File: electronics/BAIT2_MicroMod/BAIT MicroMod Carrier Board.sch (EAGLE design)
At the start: 152 parts, among them J1 SJ-43516-SMT, J10 QWIIC_RIGHT_ANGLE, J15 SM06B-SRSS-TB(LF)(SN), J2 ST-TF-003A, J4 JST_6_PIN_VERTICAL, J5 QWIIC_RIGHT_ANGLE, J6 JST 2PH, J7 MICROMOD-2222-C, SW1 SKQGADE010, SW2 SKQGADE010, U1 SGTL5000-32, U10 TSL25911, U2 AP7313, U3 3.3V, U4 3.3V, U5 BQ27441-G1, U6 BQ24074, U7 LoRa-E5-HF, U8 S-1172B33-E6T1U, U9 BOSCH_TOOLS_BME680BOSCH_TOOLS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

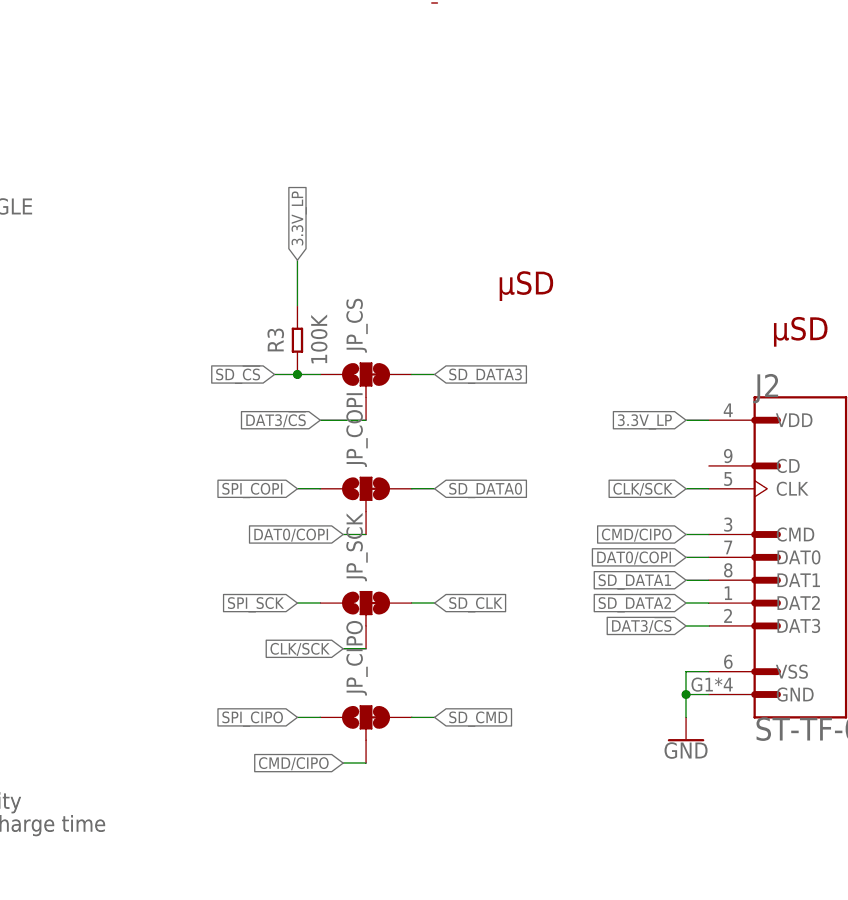
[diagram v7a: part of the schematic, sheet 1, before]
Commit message: Removes secondary options for connecting to SD card
Resolves #22
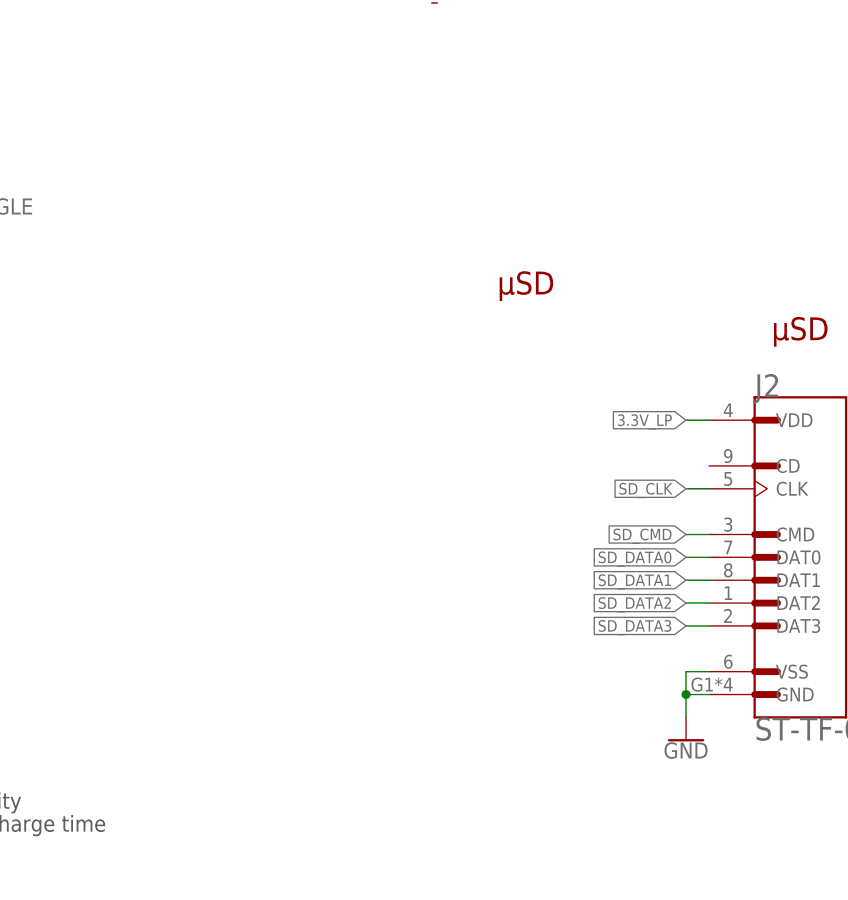
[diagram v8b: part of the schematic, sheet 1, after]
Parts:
- removed JP_CIPO, JP_COPI, JP_CS, JP_SCK: JUMPER-SMT_3_1-NC_TRACE_SILK, SparkFun-Jumpers:JUMPER-SMT_3_1-NC_TRACE_SILK
- removed R3: 100K, OPL_Resistor:SMD-RES-100K-1%-1/10W(0603)
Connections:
- removed net CLK/SCK: J2.CLK, JP_SCK.2
- removed net CMD/CIPO: J2.CMD, JP_CIPO.2
- removed net DAT0/COPI: J2.DAT0, JP_COPI.2
- removed net DAT3/!CS!: J2.DAT3, JP_CS.2
- net 3.3V_LP: no longer R3.2
- net SD_!CS!: no longer JP_CS.1, R3.1
- net SD_CLK: now also J2.CLK; no longer JP_SCK.3
- net SD_CMD: now also J2.CMD; no longer JP_CIPO.3
- net SD_DATA0: now also J2.DAT0; no longer JP_COPI.3
- net SD_DATA3: now also J2.DAT3; no longer JP_CS.3
- net SPI_CIPO: no longer JP_CIPO.1
- net SPI_COPI: no longer JP_COPI.1
- net SPI_SCK: no longer JP_SCK.1
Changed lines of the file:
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@@
 <attribute name="MPN" value="BAS16J,115"/>
 </part>
-<part name="JP_CS" library="SparkFun-Jumpers" library_urn="urn:adsk.eagle:library:528" deviceset="JUMPER-SMT_3_1-NC_TRACE" device="_SILK" package3d_urn="urn:adsk.eagle:package:39288/1" value=""/>
-<part name="JP_COPI" library="SparkFun-Jumpers" library_urn="urn:adsk.eagle:library:528" deviceset="JUMPER-SMT_3_1-NC_TRACE" device="_SILK" package3d_urn="urn:adsk.eagle:package:39288/1" value=""/>
-<part name="JP_SCK" library="SparkFun-Jumpers" library_urn="urn:adsk.eagle:library:528" deviceset="JUMPER-SMT_3_1-NC_TRACE" device="_SILK" package3d_urn="urn:adsk.eagle:package:39288/1" value=""/>
-<part name="JP_CIPO" library="SparkFun-Jumpers" library_urn="urn:adsk.eagle:library:528" deviceset="JUMPER-SMT_3_1-NC_TRACE" device="_SILK" package3d_urn="urn:adsk.eagle:package:39288/1" value=""/>
-<part name="R3" library="OPL_Resistor" library_urn="urn:adsk.eagle:library:8004883" deviceset="SMD-RES-100K-1%-1/10W(0603)" device="" package3d_urn="urn:adsk.eagle:package:8004941/1" value="100K"/>
 <part name="G1" library="Power or GND " deviceset="GND_POWER" device=""/>
 <part name="J_ASC" library="SparkFun-Jumpers" deviceset="JUMPER-SMT_2_NC_TRACE" device="_SILK" package3d_urn="urn:adsk.eagle:package:39281/1" value=""/>
@@
 <attribute name="MPN" x="345.44" y="76.2" size="1.27" layer="96" rot="R90" display="off"/>
 </instance>
-<instance part="JP_CS" gate="G$1" x="256.54" y="78.74" smashed="yes" rot="R90" grouprefs="USD">
-<attribute name="NAME" x="256.159" y="81.28" size="1.778" layer="95" font="vector" rot="R90"/>
-<attribute name="VALUE" x="256.921" y="81.28" size="1.778" layer="96" font="vector" rot="R90" align="top-left"/>
-</instance>
-<instance part="JP_COPI" gate="G$1" x="256.54" y="66.04" smashed="yes" rot="R90" grouprefs="USD">
-<attribute name="NAME" x="256.159" y="68.58" size="1.778" layer="95" font="vector" rot="R90"/>
-<attribute name="VALUE" x="256.921" y="68.58" size="1.778" layer="96" font="vector" rot="R90" align="top-left"/>
-</instance>
-<instance part="JP_SCK" gate="G$1" x="256.54" y="53.34" smashed="yes" rot="R90" grouprefs="USD">
-<attribute name="NAME" x="256.159" y="55.88" size="1.778" layer="95" font="vector" rot="R90"/>
-<attribute name="VALUE" x="256.921" y="55.88" size="1.778" layer="96" font="vector" rot="R90" align="top-left"/>
-</instance>
-<instance part="JP_CIPO" gate="G$1" x="256.54" y="40.64" smashed="yes" rot="R90" grouprefs="USD">
-<attribute name="NAME" x="256.159" y="43.18" size="1.778" layer="95" font="vector" rot="R90"/>
-<attribute name="VALUE" x="256.921" y="43.18" size="1.778" layer="96" font="vector" rot="R90" align="top-left"/>
-</instance>
-<instance part="R3" gate="G$1" x="248.92" y="82.55" smashed="yes" rot="R90" grouprefs="USD">
-<attribute name="NAME" x="247.396" y="82.55" size="1.778" layer="95" font="vector" rot="R90" align="bottom-center"/>
-<attribute name="VALUE" x="250.444" y="82.55" size="1.778" layer="96" font="vector" rot="R90" align="top-center"/>
-</instance>
 <instance part="G1" gate="G$1" x="264.16" y="121.92" smashed="yes" grouprefs="WIRELESS"/>
 <instance part="J_ASC" gate="G$1" x="373.38" y="154.94" smashed="yes" rot="R90" grouprefs="WIRELESS">
@@
 <label x="73.66" y="215.9" size="1.27" layer="95" xref="yes" grouprefs="MICROMOD"/>
 </segment>
-<segment>
-<pinref part="JP_SCK" gate="G$1" pin="1"/>
-<wire x1="251.46" y1="53.34" x2="248.92" y2="53.34" width="0.1524" layer="91" grouprefs="USD"/>
-<label x="248.92" y="53.34" size="1.27" layer="95" rot="R180" xref="yes" grouprefs="USD"/>
-</segment>
 </net>
 <net name="SD_!CS!" class="2">
@@
 <wire x1="71.12" y1="208.28" x2="73.66" y2="208.28" width="0.1524" layer="91" grouprefs="MICROMOD"/>
 <label x="73.66" y="208.28" size="1.27" layer="95" xref="yes" grouprefs="MICROMOD"/>
-</segment>
-<segment>
-<pinref part="JP_CS" gate="G$1" pin="1"/>
-<wire x1="248.92" y1="78.74" x2="246.38" y2="78.74" width="0.1524" layer="91" grouprefs="USD"/>
-<label x="246.38" y="78.74" size="1.27" layer="95" rot="R180" xref="yes" grouprefs="USD"/>
-<pinref part="R3" gate="G$1" pin="1"/>
-<junction x="248.92" y="78.74" grouprefs="USD"/>
-<wire x1="248.92" y1="78.74" x2="251.46" y2="78.74" width="0.1524" layer="91" grouprefs="USD"/>
 </segment>
 </net>
@@
 <label x="73.66" y="213.36" size="1.27" layer="95" xref="yes" grouprefs="MICROMOD"/>
 </segment>
-<segment>
-<pinref part="JP_COPI" gate="G$1" pin="1"/>
-<wire x1="251.46" y1="66.04" x2="248.92" y2="66.04" width="0.1524" layer="91" grouprefs="USD"/>
-<label x="248.92" y="66.04" size="1.27" layer="95" rot="R180" xref="yes" grouprefs="USD"/>
-</segment>
 </net>
 <net name="SPI_CIPO" class="2">
@@
 <wire x1="71.12" y1="210.82" x2="73.66" y2="210.82" width="0.1524" layer="91" grouprefs="MICROMOD"/>
 <label x="73.66" y="210.82" size="1.27" layer="95" xref="yes" grouprefs="MICROMOD"/>
-</segment>
-<segment>
-<pinref part="JP_CIPO" gate="G$1" pin="1"/>
-<wire x1="251.46" y1="40.64" x2="248.92" y2="40.64" width="0.1524" layer="91" grouprefs="USD"/>
-<label x="248.92" y="40.64" size="1.27" layer="95" rot="R180" xref="yes" grouprefs="USD"/>
 </segment>
 </net>
@@
 </net>
 <net name="3.3V_LP" class="1">
-<segment>
-<pinref part="R3" gate="G$1" pin="2"/>
-<wire x1="248.92" y1="86.36" x2="248.92" y2="91.44" width="0.1524" layer="91" grouprefs="USD"/>
-<label x="248.92" y="91.44" size="1.27" layer="95" rot="R90" xref="yes" grouprefs="USD"/>
-</segment>
 <segment>
 <pinref part="C6" gate="G$1" pin="1"/>
@@
 </segment>
 <segment>
-<pinref part="JP_SCK" gate="G$1" pin="3"/>
-<wire x1="261.62" y1="53.34" x2="264.16" y2="53.34" width="0.1524" layer="91" grouprefs="USD"/>
-<label x="264.16" y="53.34" size="1.27" layer="95" xref="yes" grouprefs="USD"/>
+<pinref part="J2" gate="G$1" pin="CLK"/>
+<wire x1="294.64" y1="66.04" x2="292.1" y2="66.04" width="0.1524" layer="91" grouprefs="USD"/>
+<label x="292.1" y="66.04" size="1.27" layer="95" rot="R180" xref="yes" grouprefs="USD"/>
 </segment>
 </net>
@@
 </segment>
 <segment>
-<pinref part="JP_CIPO" gate="G$1" pin="3"/>
-<wire x1="261.62" y1="40.64" x2="264.16" y2="40.64" width="0.1524" layer="91" grouprefs="USD"/>
-<label x="264.16" y="40.64" size="1.27" layer="95" xref="yes" grouprefs="USD"/>
+<pinref part="J2" gate="G$1" pin="CMD"/>
+<wire x1="294.64" y1="60.96" x2="292.1" y2="60.96" width="0.1524" layer="91" grouprefs="USD"/>
+<label x="292.1" y="60.96" size="1.27" layer="95" rot="R180" xref="yes" grouprefs="USD"/>
 </segment>
 </net>
@@
 </segment>
 <segment>
-<pinref part="JP_COPI" gate="G$1" pin="3"/>
-<wire x1="261.62" y1="66.04" x2="264.16" y2="66.04" width="0.1524" layer="91" grouprefs="USD"/>
-<label x="264.16" y="66.04" size="1.27" layer="95" xref="yes" grouprefs="USD"/>
+<pinref part="J2" gate="G$1" pin="DAT0"/>
+<wire x1="294.64" y1="58.42" x2="292.1" y2="58.42" width="0.1524" layer="91" grouprefs="USD"/>
+<label x="292.1" y="58.42" size="1.27" layer="95" rot="R180" xref="yes" grouprefs="USD"/>
 </segment>
 </net>
@@
 </segment>
 <segment>
-<pinref part="JP_CS" gate="G$1" pin="3"/>
-<wire x1="261.62" y1="78.74" x2="264.16" y2="78.74" width="0.1524" layer="91" grouprefs="USD"/>
-<label x="264.16" y="78.74" size="1.27" layer="95" xref="yes" grouprefs="USD"/>
-</segment>
-</net>
-<net name="DAT3/!CS!" class="2">
-<segment>
-<pinref part="JP_CS" gate="G$1" pin="2"/>
-<wire x1="256.54" y1="73.66" x2="251.46" y2="73.66" width="0.1524" layer="91" grouprefs="USD"/>
-<label x="251.46" y="73.66" size="1.27" layer="95" rot="R180" xref="yes" grouprefs="USD"/>
-</segment>
-<segment>
 <pinref part="J2" gate="G$1" pin="DAT3"/>
 <wire x1="294.64" y1="50.8" x2="292.1" y2="50.8" width="0.1524" layer="91" grouprefs="USD"/>
@@
 </segment>
 </net>
-<net name="CMD/CIPO" class="2">
-<segment>
-<pinref part="JP_CIPO" gate="G$1" pin="2"/>
-<wire x1="256.54" y1="35.56" x2="254" y2="35.56" width="0.1524" layer="91" grouprefs="USD"/>
-<label x="254" y="35.56" size="1.27" layer="95" rot="R180" xref="yes" grouprefs="USD"/>
-</segment>
-<segment>
-<pinref part="J2" gate="G$1" pin="CMD"/>
-<wire x1="294.64" y1="60.96" x2="292.1" y2="60.96" width="0.1524" layer="91" grouprefs="USD"/>
-<label x="292.1" y="60.96" size="1.27" layer="95" rot="R180" xref="yes" grouprefs="USD"/>
-</segment>
-</net>
-<net name="CLK/SCK" class="2">
-<segment>
-<pinref part="JP_SCK" gate="G$1" pin="2"/>
-<wire x1="256.54" y1="48.26" x2="254" y2="48.26" width="0.1524" layer="91" grouprefs="USD"/>
-<label x="254" y="48.26" size="1.27" layer="95" rot="R180" xref="yes" grouprefs="USD"/>
-</segment>
-<segment>
-<pinref part="J2" gate="G$1" pin="CLK"/>
-<wire x1="294.64" y1="66.04" x2="292.1" y2="66.04" width="0.1524" layer="91" grouprefs="USD"/>
-<label x="292.1" y="66.04" size="1.27" layer="95" rot="R180" xref="yes" grouprefs="USD"/>
-</segment>
-</net>
-<net name="DAT0/COPI" class="2">
-<segment>
-<pinref part="JP_COPI" gate="G$1" pin="2"/>
-<wire x1="256.54" y1="60.96" x2="254" y2="60.96" width="0.1524" layer="91" grouprefs="USD"/>
-<label x="254" y="60.96" size="1.27" layer="95" rot="R180" xref="yes" grouprefs="USD"/>
-</segment>
-<segment>
-<pinref part="J2" gate="G$1" pin="DAT0"/>
-<wire x1="294.64" y1="58.42" x2="292.1" y2="58.42" width="0.1524" layer="91" grouprefs="USD"/>
-<label x="292.1" y="58.42" size="1.27" layer="95" rot="R180" xref="yes" grouprefs="USD"/>
-</segment>
-</net>
